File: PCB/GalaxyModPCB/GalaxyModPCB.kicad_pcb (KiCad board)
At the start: 2 copper layers, 63.5 x 38.2 mm, 65 parts, among them J1 LED RGBW Connector, J2 USB to UART, J3 Motor Connector, J4 Projector Connector, J5 Debug Header, J6 Power Header, J7 Boot mode, Q1 IRLML0030, Q2 IRLML0030, Q3 IRLML0030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

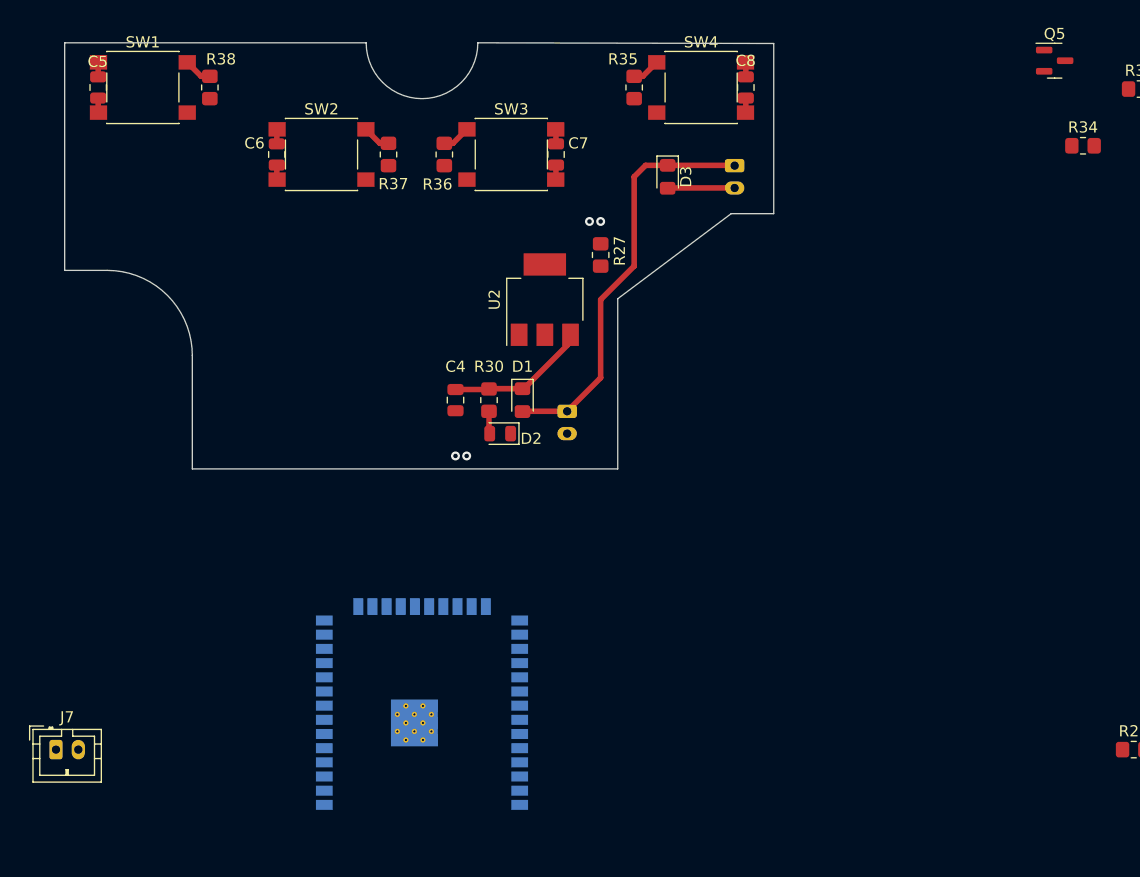
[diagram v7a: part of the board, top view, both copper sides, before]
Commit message: Connected power circuitry
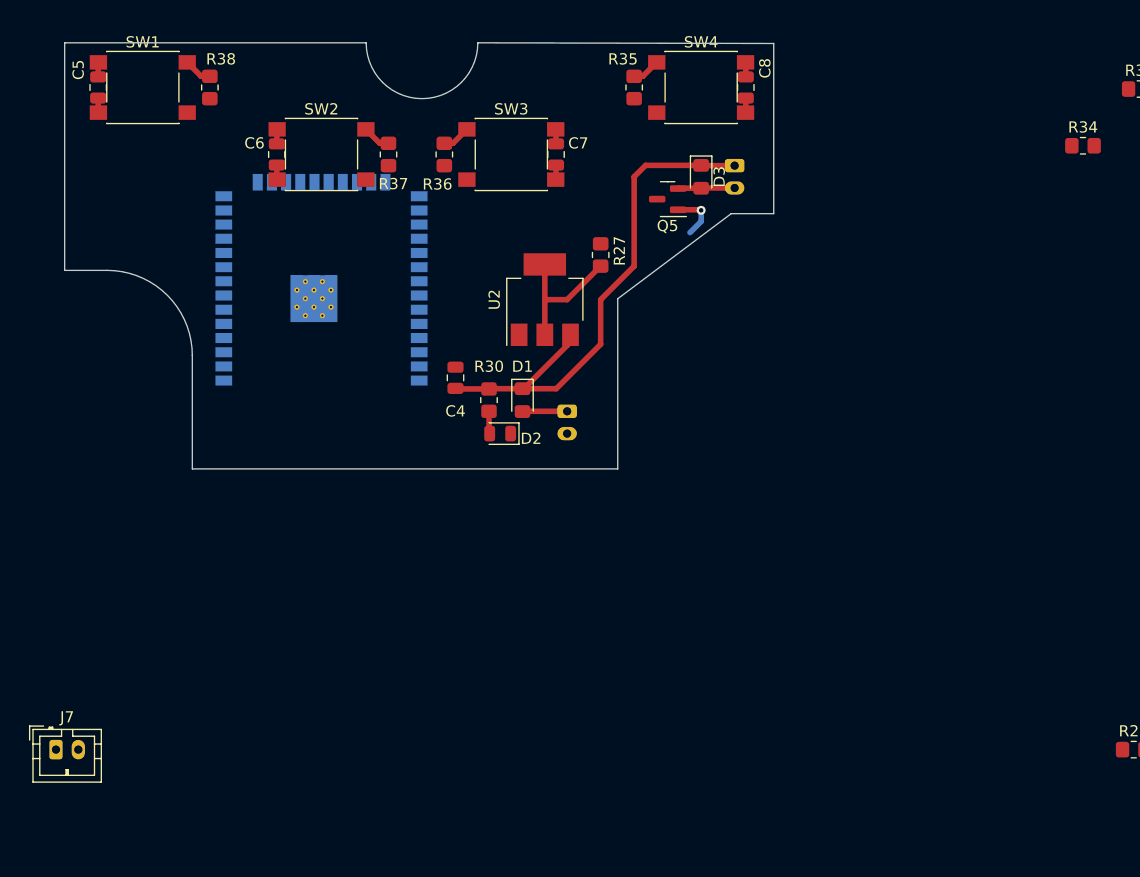
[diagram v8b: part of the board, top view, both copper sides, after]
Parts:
- moved U1 39.1 mm to (133.0, 73.0)
- moved Q5 36.8 mm to (164.0, 65.0), turned to 180 degrees
- moved D3 3.00 mm to (167.0, 63.0)
- moved C4 2.00 mm to (145.0, 81.0), turned to 90 degrees
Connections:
- C4 pad 1: Net-(C4-Pad1) -> Net-(D3-Pad1)
- D1 pad 1: Net-(C4-Pad1) -> Net-(D3-Pad1)
- D1 pad 2: Net-(J1-Pad1) -> Net-(D1-Pad2)
- D3 pad 1: Net-(J1-Pad1) -> Net-(D3-Pad1)
- J1 pad 1: Net-(J1-Pad1) -> Net-(D3-Pad1)
- J3 pad 1: Net-(J1-Pad1) -> Net-(D3-Pad1)
- J6 pad 1: Net-(J1-Pad1) -> Net-(D1-Pad2)
- R30 pad 2: Net-(C4-Pad1) -> Net-(D3-Pad1)
- U2 pad 3: Net-(C4-Pad1) -> Net-(D3-Pad1)
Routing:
- net Net-(D3-Pad1): track 0.00 -> 46.2 mm
- net Net-(J1-Pad1): track 36.9 -> 0.00 mm
- net Net-(R27-Pad1): track 0.00 -> 12.5 mm
- net Net-(C4-Pad1): track 11.8 -> 0.00 mm
- net Net-(Q5-Pad1): track 0.00 -> 4.50 mm, vias 0 -> 1
- net Net-(D1-Pad2): track 0.00 -> 4.01 mm
- net Net-(J3-Pad2): track 6.01 -> 5.08 mm
- net (no net): vias 4 -> 0
